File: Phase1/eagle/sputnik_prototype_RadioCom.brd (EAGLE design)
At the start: 100 x 80 mm, 73 parts, among them Y1 32MHz

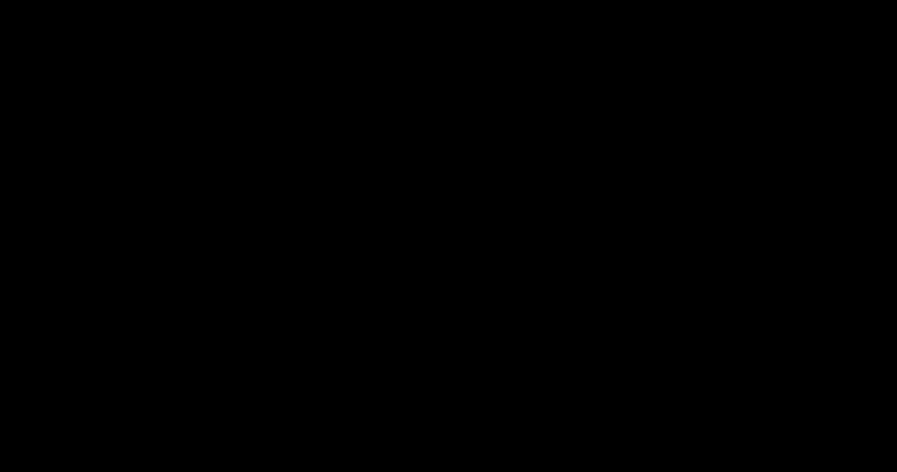
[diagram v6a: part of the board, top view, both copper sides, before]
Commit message: Added 22 pinout, no footprint yet, also did RF_GND
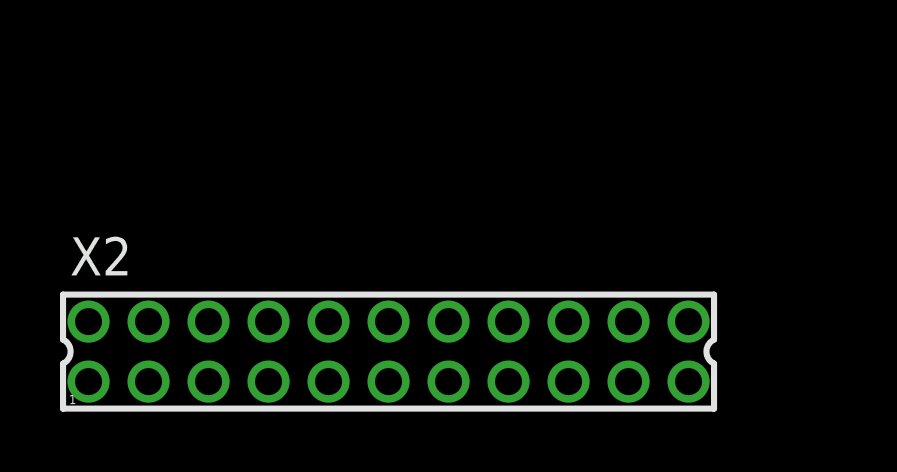
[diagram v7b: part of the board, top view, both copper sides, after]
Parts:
- added X2: 332-22, con-garry:332-22
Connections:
- new net N$32: KW0X.50, X2.2
- new net N$33: KW0X.5, X2.3
- new net N$35: KW0X.6, X2.4
- new net N$36: KW0X.7, X2.5
- new net N$37: KW0X.8, X2.6
- new net N$38: KW0X.9, X2.7
- new net N$4: KW0X.49, X2.1
- new net PA_EN: KW0X.34, U$9.5
- new net PTB0: KW0X.17
- new net PTB1: KW0X.18, X2.12
- new net PTB17: KW0X.22, X2.14
- new net PTB2: KW0X.21, X2.13
- new net PTBO: X2.11
- new net PTC1: KW0X.24, X2.15
- new net PTC2: KW0X.25, X2.16
- new net PTC3: KW0X.26, X2.17
- new net PTC4: KW0X.23, X2.18
- new net PTC5: KW0X.59, X2.19
- new net PTC6: KW0X.60, X2.20
- new net RF_RESET: X2.21
- new net SOMETHING: KW0X.48
- net GND: now also U$9.4
- net PE0/UART0RX: now also X2.8
- net PE1/UART0TX: now also X2.9
- net PE3: now also X2.10
- net V+: now also X2.22; no longer U$9.5

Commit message: Updated Enable lines, switch is gonna be moved to SysCon board
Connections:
- new net LNA_EN: KW0X.57, U$7.3
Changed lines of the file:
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@@
 <contactref element="X2" pad="21"/>
+</signal>
+<signal name="LNA_EN">
+<contactref element="KW0X" pad="57"/>
+<contactref element="U$7" pad="3"/>
+<wire x1="39.85" y1="38.58" x2="61.435" y2="28.32" width="0" layer="19" extent="1-1"/>
 </signal>
 </signals>
